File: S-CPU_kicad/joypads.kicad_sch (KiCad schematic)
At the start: 280 parts, among them U33 OR_2, U38 OR_2

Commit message: Schematics update.
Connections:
- net wMASS_RST is gone; now on net wMASS_~{JP_RST}: KBKC.1 (~{RESET}), KBKC.5 (~{RESET}), KBLJ.1 (~{RESET}), KBLJ.5 (~{RESET}), KBMV.1 (~{RESET}), KBMV.5 (~{RESET}), RBSA.1 (~{RESET}), RBSA.5 (~{RESET}), RBTV.1 (~{RESET}), RBTV.1 (~{RESET}), RBTV.5 (~{RESET}), RBTV.5 (~{RESET})
- net wMASS_~{JP_RST}: now reaches KAVS.1 (~{RESET}), KAVS.5 (~{RESET}), KBGM.1 (~{RESET}), KBGM.5 (~{RESET}), KBGO.1 (~{RESET}), KBGO.5 (~{RESET}), KBIE.1 (~{RESET}), KBIE.5 (~{RESET}), KBIF.1 (~{RESET}), KBIF.5 (~{RESET}), KBKC.1 (~{RESET}), KBKC.5 (~{RESET}), KBLJ.1 (~{RESET}), KBLJ.5 (~{RESET}), KBMV.1 (~{RESET}), KBMV.5 (~{RESET})
- net wNBRL_wNBQA_XIN/4 renamed wNBRL_wNBQA_~{XIN/4}
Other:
- company: Regis Galland -> Author: Regis Galland
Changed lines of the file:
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@@
     (date "2023-06-14")
     (rev "0.1")
-    (company "Regis Galland")
+    (company "Author: Regis Galland")
   )
   (junction (at 524.51 484.505) (diameter 0) (color 0 0 0 0)
@@
   (junction (at 494.03 487.045) (diameter 0) (color 0 0 0 0)
   )
+  (junction (at 146.05 552.45) (diameter 0) (color 0 0 0 0)
+  )
   (junction (at 269.875 433.705) (diameter 0) (color 0 0 0 0)
   )
@@
     (stroke (width 0) (type default))
   )
-  (wire (pts (xy 146.05 445.77) (xy 146.05 463.55))
-    (stroke (width 0) (type default))
-  )
   (wire (pts (xy 106.68 316.23) (xy 116.84 316.23))
     (stroke (width 0) (type default))
@@
     (stroke (width 0) (type default))
   )
-  (wire (pts (xy 327.66 478.155) (xy 327.66 479.425))
+  (wire (pts (xy 146.05 516.89) (xy 146.05 499.11))
     (stroke (width 0) (type default))
   )
-  (wire (pts (xy 146.05 499.11) (xy 146.05 516.89))
+  (wire (pts (xy 327.66 478.155) (xy 327.66 479.425))
     (stroke (width 0) (type default))
   )
@@
     (stroke (width 0) (type default))
   )
+  (wire (pts (xy 146.05 463.55) (xy 146.05 445.77))
+    (stroke (width 0) (type default))
+  )
   (wire (pts (xy 669.29 502.285) (xy 675.64 502.285))
     (stroke (width 0) (type default))
@@
     (stroke (width 0) (type default))
   )
-  (wire (pts (xy 278.13 189.23) (xy 278.13 201.295))
+  (wire (pts (xy 278.13 189.23) (xy 278.13 200.66))
     (stroke (width 0) (type default))
   )
@@
     (stroke (width 0) (type default))
   )
-  (wire (pts (xy 146.05 516.89) (xy 146.05 534.67))
-    (stroke (width 0) (type default))
-  )
   (wire (pts (xy 635.635 395.605) (xy 656.59 395.605))
     (stroke (width 0) (type default))
@@
     (stroke (width 0) (type default))
   )
+  (wire (pts (xy 146.05 534.67) (xy 146.05 516.89))
+    (stroke (width 0) (type default))
+  )
   (wire (pts (xy 334.01 466.725) (xy 340.36 466.725))
     (stroke (width 0) (type default))
@@
     (stroke (width 0) (type default))
   )
-  (wire (pts (xy 146.05 463.55) (xy 146.05 481.33))
-    (stroke (width 0) (type default))
-  )
   (wire (pts (xy 496.57 299.72) (xy 524.51 299.72))
     (stroke (width 0) (type default))
@@
     (stroke (width 0) (type default))
   )
-  (wire (pts (xy 262.255 201.295) (xy 278.13 201.295))
+  (wire (pts (xy 254 200.66) (xy 278.13 200.66))
     (stroke (width 0) (type default))
   )
@@
     (stroke (width 0) (type default))
   )
+  (wire (pts (xy 117.475 571.5) (xy 146.05 571.5))
+    (stroke (width 0) (type default))
+  )
   (wire (pts (xy 384.175 388.62) (xy 384.175 400.685))
     (stroke (width 0) (type default))
@@
     (stroke (width 0) (type default))
   )
+  (wire (pts (xy 146.05 552.45) (xy 146.05 534.67))
+    (stroke (width 0) (type default))
+  )
   (wire (pts (xy 116.84 355.6) (xy 111.76 355.6))
     (stroke (width 0) (type default))
@@
     (stroke (width 0) (type default))
   )
-  (wire (pts (xy 146.05 534.67) (xy 146.05 552.45))
-    (stroke (width 0) (type default))
-  )
   (wire (pts (xy 535.94 318.135) (xy 535.94 335.915))
     (stroke (width 0) (type default))
@@
     (stroke (width 0) (type default))
   )
+  (wire (pts (xy 146.05 571.5) (xy 146.05 552.45))
+    (stroke (width 0) (type default))
+  )
   (wire (pts (xy 389.255 413.385) (xy 386.715 413.385))
     (stroke (width 0) (type default))
@@
     (stroke (width 0) (type default))
   )
+  (wire (pts (xy 146.05 481.33) (xy 146.05 463.55))
+    (stroke (width 0) (type default))
+  )
   (wire (pts (xy 635.635 413.385) (xy 635.635 424.18))
     (stroke (width 0) (type default))
@@
     (effects (font (size 5 5) (thickness 1) bold) (justify left bottom))
   )
-  (label "D[0..7]" (at 142.875 565.15 0) (fields_autoplaced)
+  (label "D[0..7]" (at 151.765 565.15 0) (fields_autoplaced)
     (effects (font (size 1.27 1.27)) (justify left bottom))
   )
@@
     (effects (font (size 1.27 1.27)) (justify right bottom))
   )
-  (label "wMASS_RST" (at 262.255 201.295 0) (fields_autoplaced)
+  (label "wMASS_~{JP_RST}" (at 254 200.66 0) (fields_autoplaced)
     (effects (font (size 1.27 1.27)) (justify left bottom))
   )
@@
     (effects (font (size 1.27 1.27)) (justify right bottom))
   )
+  (label "wMASS_~{JP_RST}" (at 117.475 571.5 0) (fields_autoplaced)
+    (effects (font (size 1.27 1.27)) (justify left bottom))
+  )
   (label "JPO4" (at 203.835 496.57 180) (fields_autoplaced)
     (effects (font (size 1.27 1.27)) (justify right bottom))
@@
     (effects (font (size 1.27 1.27)) (justify right bottom))
   )
-  (label "wMASS_RST" (at 549.91 212.725 0) (fields_autoplaced)
+  (label "wMASS_~{JP_RST}" (at 549.91 212.725 0) (fields_autoplaced)
     (effects (font (size 1.27 1.27)) (justify left bottom))
   )
@@
     (effects (font (size 1.27 1.27)) (justify right))
   )
-  (hierarchical_label "wNBRL_wNBQA_XIN{slash}4" (shape input) (at 213.36 85.725 180) (fields_autoplaced)
+  (hierarchical_label "wNBRL_wNBQA_~{XIN{slash}4}" (shape input) (at 213.36 85.725 180) (fields_autoplaced)
     (effects (font (size 1.27 1.27)) (justify right))
   )
@@
     (effects (font (size 1.27 1.27)) (justify right))
   )
-  (hierarchical_label "wMASS_RST" (shape input) (at 262.255 201.295 180) (fields_autoplaced)
+  (hierarchical_label "wMASS_~{JP_RST}" (shape input) (at 254 200.66 180) (fields_autoplaced)
     (effects (font (size 1.27 1.27)) (justify right))
   )

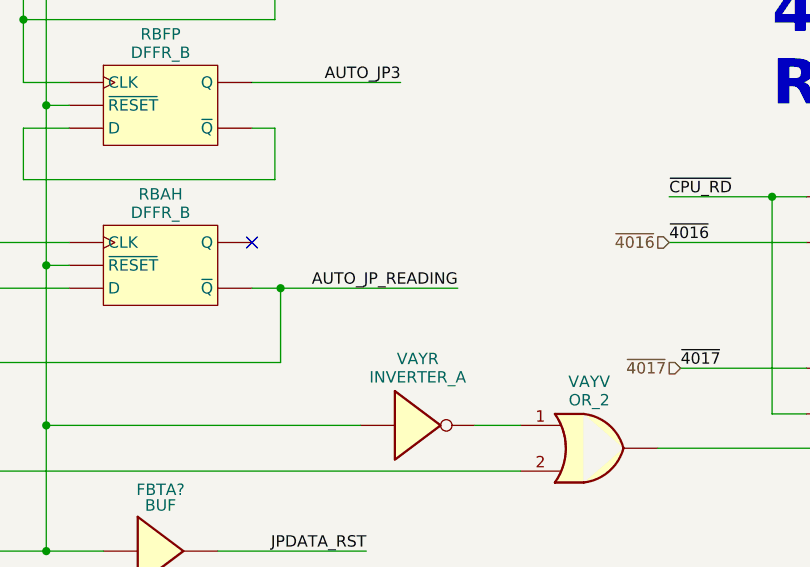
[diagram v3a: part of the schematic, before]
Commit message: Schematics tidying in progress.
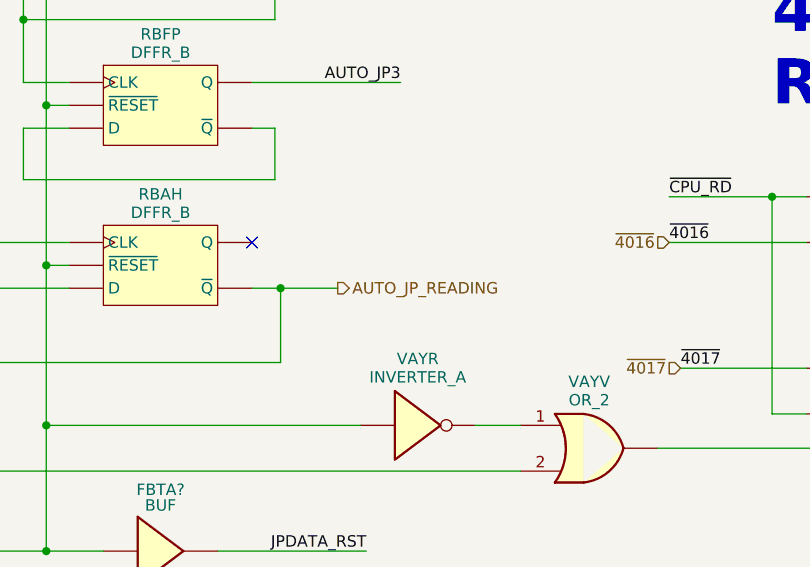
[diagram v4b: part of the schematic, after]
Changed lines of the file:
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@@
   (title_block
     (title "SNES S-CPU Schematics ")
-    (date "2023-06-14")
+    (date "2023-10-19")
     (rev "0.1")
     (company "Author: Regis Galland")
@@
     (stroke (width 0) (type default))
   )
-  (wire (pts (xy 372.11 109.855) (xy 352.425 109.855))
+  (wire (pts (xy 358.775 109.855) (xy 352.425 109.855))
     (stroke (width 0) (type default))
   )
@@
     (effects (font (size 1.27 1.27)) (justify left bottom))
   )
-  (label "AUTO_JP_READING" (at 372.11 109.855 180) (fields_autoplaced)
-    (effects (font (size 1.27 1.27)) (justify right bottom))
-  )
   (label "JPO3" (at 203.835 478.79 180) (fields_autoplaced)
     (effects (font (size 1.27 1.27)) (justify right bottom))
@@
     (effects (font (size 1.27 1.27)) (justify right))
   )
+  (hierarchical_label "AUTO_JP_READING" (shape output) (at 358.775 109.855 0) (fields_autoplaced)
+    (effects (font (size 1.27 1.27)) (justify left))
+  )
   (symbol (lib_id "Ricoh_Cells:DFFR_A") (at 287.655 273.685 0) (unit 1)

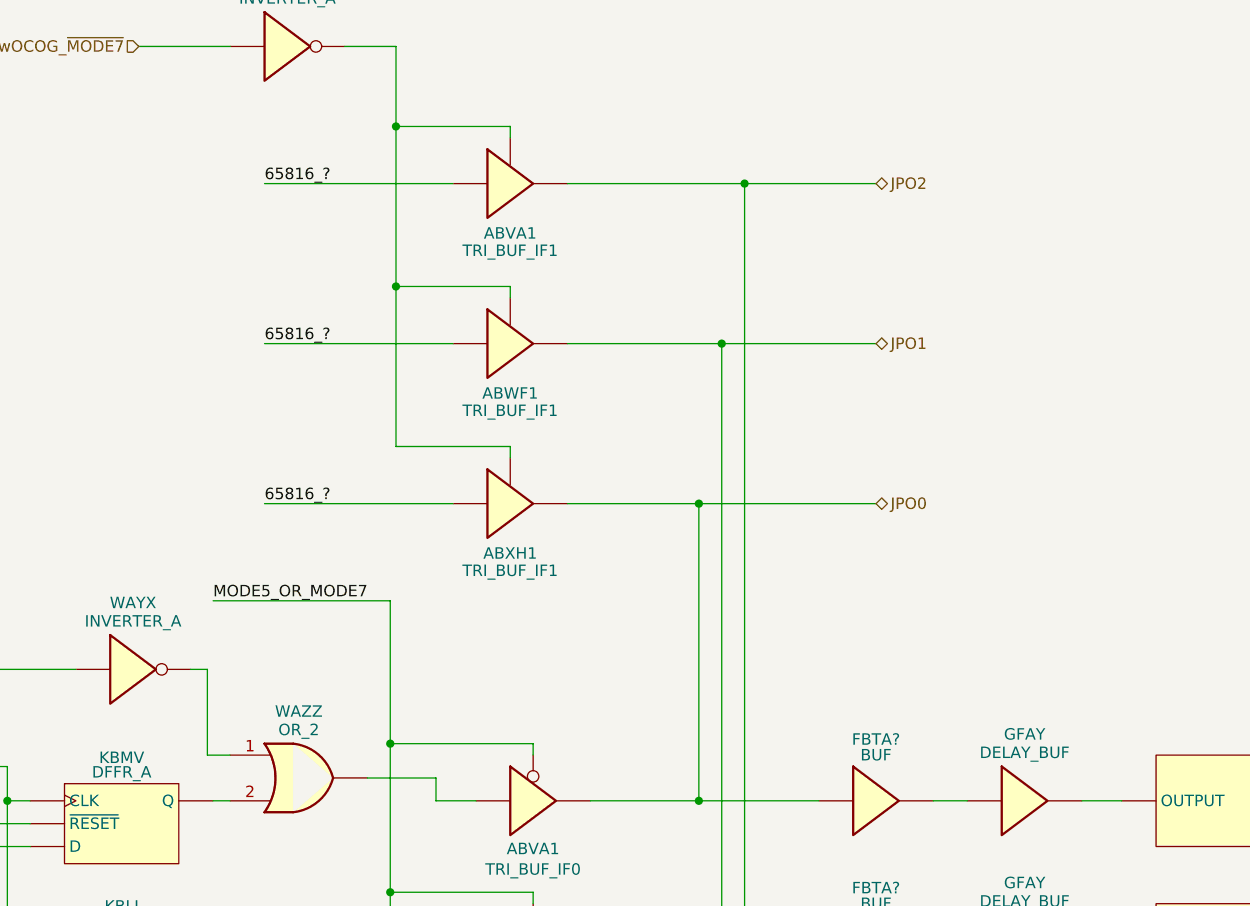
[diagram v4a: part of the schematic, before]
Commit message: Big update on the hierarchical sheet. DMA section update too.
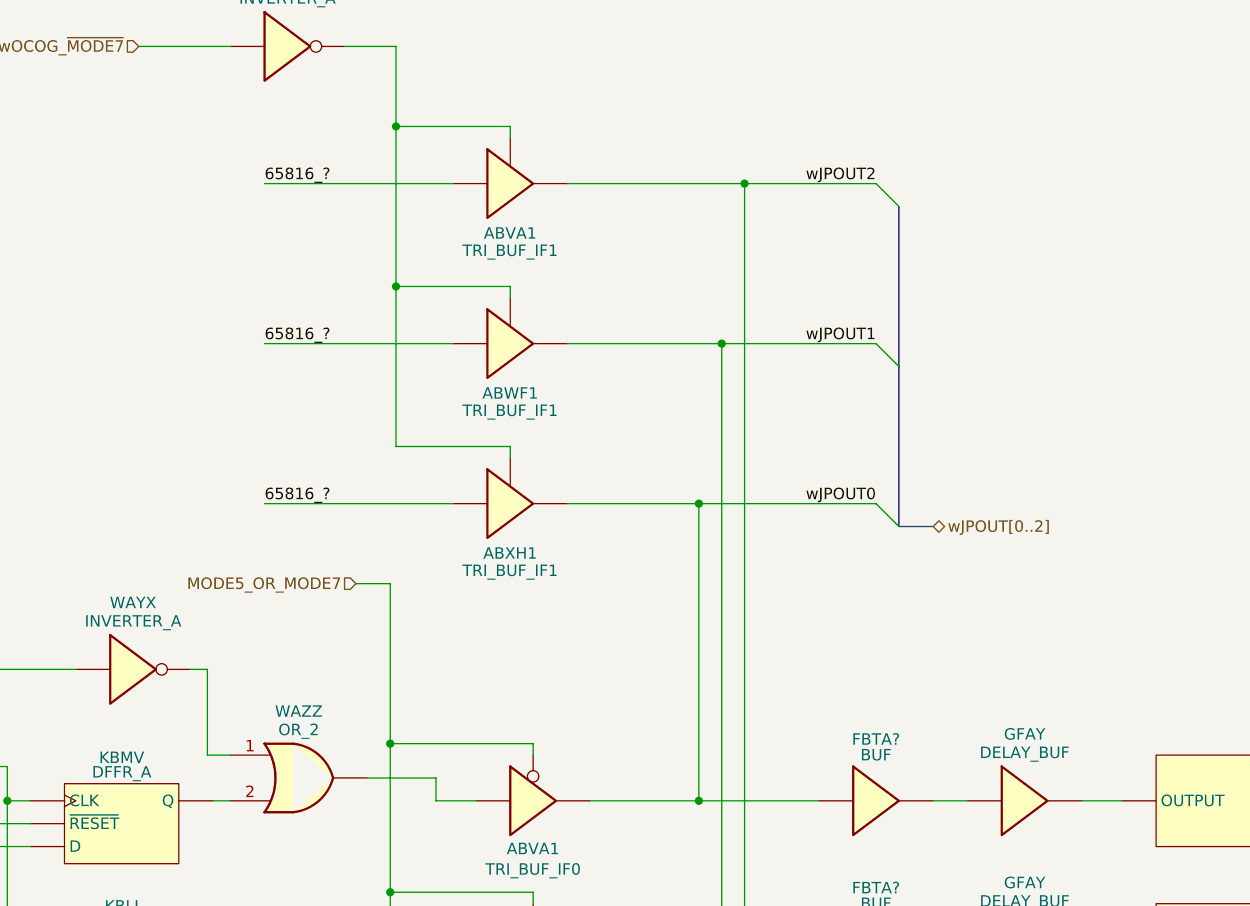
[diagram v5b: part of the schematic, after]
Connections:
- net JPO0: no longer ABVA1.4, ABXH1.4, FBTA?.1
- net JPO1: no longer ABVA1.4, ABWF1.4, FBTA?.1
- net JPO2: no longer ABVA1.4, ABVA1.4, FBTA?.1
- new net wJPOUT0: ABVA1.4, ABXH1.4, FBTA?.1
- new net wJPOUT1: ABVA1.4, ABWF1.4, FBTA?.1
- new net wJPOUT2: ABVA1.4, ABVA1.4, FBTA?.1
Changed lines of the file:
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@@
   (title_block
     (title "SNES S-CPU Schematics ")
-    (date "2023-10-19")
+    (date "2023-10-21")
     (rev "0.1")
     (company "Author: Regis Galland")
@@
     (stroke (width 0) (type default))
   )
+  (bus_entry (at 666.75 98.425) (size 2.54 2.54)
+    (stroke (width 0) (type default))
+  )
   (bus_entry (at 675.64 271.145) (size 2.54 2.54)
     (stroke (width 0) (type default))
@@
     (stroke (width 0) (type default))
   )
+  (bus_entry (at 666.75 116.205) (size 2.54 2.54)
+    (stroke (width 0) (type default))
+  )
   (bus_entry (at 452.12 395.605) (size 2.54 2.54)
     (stroke (width 0) (type default))
@@
     (stroke (width 0) (type default))
   )
+  (bus_entry (at 666.75 133.985) (size 2.54 2.54)
+    (stroke (width 0) (type default))
+  )
   (bus_entry (at 203.835 514.35) (size 2.54 -2.54)
     (stroke (width 0) (type default))
@@
     (stroke (width 0) (type default))
   )
+  (bus (pts (xy 669.29 136.525) (xy 673.1 136.525))
+    (stroke (width 0) (type default))
+  )
   (wire (pts (xy 93.98 304.165) (xy 116.84 304.165))
     (stroke (width 0) (type default))
@@
     (stroke (width 0) (type default))
   )
+  (bus (pts (xy 669.29 118.745) (xy 669.29 136.525))
+    (stroke (width 0) (type default))
+  )
   (wire (pts (xy 617.855 167.005) (xy 622.3 167.005))
     (stroke (width 0) (type default))
@@
     (stroke (width 0) (type default))
   )
-  (wire (pts (xy 612.775 144.78) (xy 612.775 160.655))
+  (wire (pts (xy 612.775 142.875) (xy 612.775 160.655))
     (stroke (width 0) (type default))
   )
@@
     (stroke (width 0) (type default))
   )
-  (wire (pts (xy 612.775 144.78) (xy 593.09 144.78))
+  (wire (pts (xy 612.775 142.875) (xy 608.965 142.875))
     (stroke (width 0) (type default))
   )
@@
     (stroke (width 0) (type default))
   )
+  (bus (pts (xy 669.29 100.965) (xy 669.29 118.745))
+    (stroke (width 0) (type default))
+  )
   (wire (pts (xy 635.635 324.485) (xy 635.635 335.28))
     (stroke (width 0) (type default))
@@
     (effects (font (size 1.27 1.27)) (justify right bottom))
   )
+  (label "wJPOUT1" (at 666.75 116.205 180) (fields_autoplaced)
+    (effects (font (size 1.27 1.27)) (justify right bottom))
+  )
   (label "D2" (at 340.36 306.705 180) (fields_autoplaced)
     (effects (font (size 1.27 1.27)) (justify right bottom))
@@
     (effects (font (size 1.27 1.27)) (justify left bottom))
   )
-  (label "MODE5_OR_MODE7" (at 593.09 144.78 0) (fields_autoplaced)
-    (effects (font (size 1.27 1.27)) (justify left bottom))
-  )
   (label "wJP2I0" (at 723.9 370.205 0) (fields_autoplaced)
     (effects (font (size 1.27 1.27)) (justify left bottom))
@@
     (effects (font (size 1.27 1.27)) (justify left bottom))
   )
+  (label "wJPOUT2" (at 666.75 98.425 180) (fields_autoplaced)
+    (effects (font (size 1.27 1.27)) (justify right bottom))
+  )
   (label "D5" (at 564.515 360.045 180) (fields_autoplaced)
     (effects (font (size 1.27 1.27)) (justify right bottom))
@@
     (effects (font (size 1.27 1.27)) (justify right bottom))
   )
+  (label "wJPOUT0" (at 666.75 133.985 180) (fields_autoplaced)
+    (effects (font (size 1.27 1.27)) (justify right bottom))
+  )
   (label "wMASS_~{JP_RST}" (at 549.91 212.725 0) (fields_autoplaced)
     (effects (font (size 1.27 1.27)) (justify left bottom))
@@
     (effects (font (size 1.27 1.27)) (justify right))
   )
-  (hierarchical_label "JPO0" (shape tri_state) (at 666.75 133.985 0) (fields_autoplaced)
-    (effects (font (size 1.27 1.27)) (justify left))
-  )
   (hierarchical_label "~{wRDY}" (shape input) (at 165.1 86.995 180) (fields_autoplaced)
     (effects (font (size 1.27 1.27)) (justify right))
@@
     (effects (font (size 1.27 1.27)) (justify right))
   )
-  (hierarchical_label "JPO1" (shape tri_state) (at 666.75 116.205 0) (fields_autoplaced)
+  (hierarchical_label "wJPOUT[0..2]" (shape tri_state) (at 673.1 136.525 0) (fields_autoplaced)
     (effects (font (size 1.27 1.27)) (justify left))
   )
@@
     (effects (font (size 1.27 1.27)) (justify right))
   )
+  (hierarchical_label "MODE5_OR_MODE7" (shape input) (at 608.965 142.875 180) (fields_autoplaced)
+    (effects (font (size 1.27 1.27)) (justify right))
+  )
   (hierarchical_label "wOCOG_~{MODE7}" (shape input) (at 584.835 83.185 180) (fields_autoplaced)
     (effects (font (size 1.27 1.27)) (justify right))
@@
     (effects (font (size 1.27 1.27)) (justify right))
   )
-  (hierarchical_label "JPO2" (shape tri_state) (at 666.75 98.425 0) (fields_autoplaced)
-    (effects (font (size 1.27 1.27)) (justify left))
-  )
   (hierarchical_label "wVBLANK" (shape input) (at 254 191.77 180) (fields_autoplaced)
